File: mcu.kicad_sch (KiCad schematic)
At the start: 21 parts, among them J2 Conn_ARM_SWD_TagConnect_TC2030, SW1 SW_Push, U3 STM32L053R8Tx

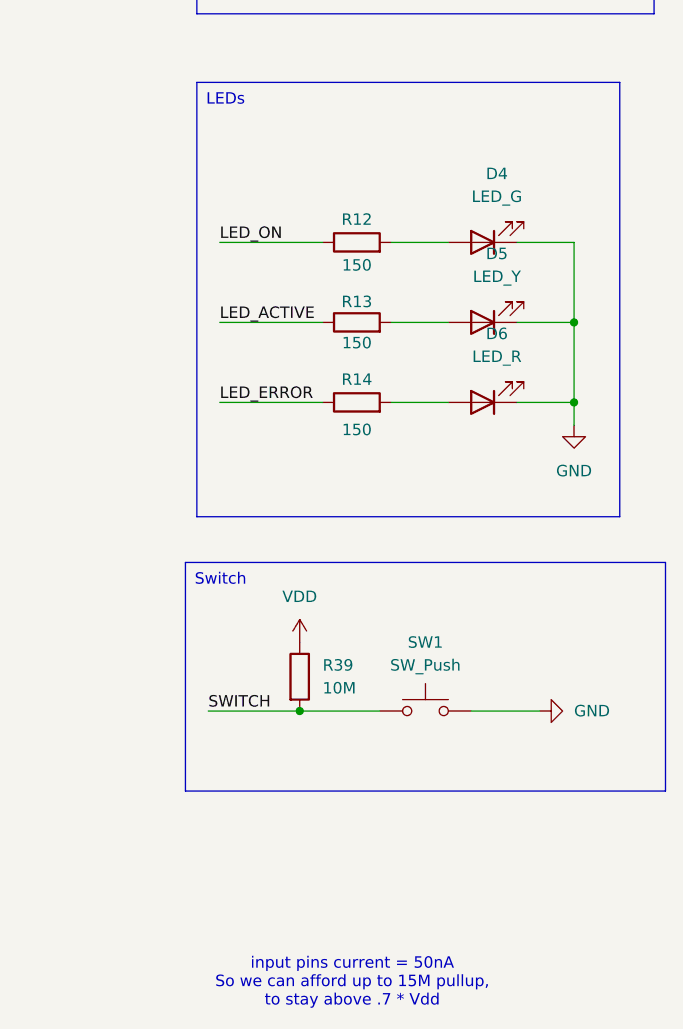
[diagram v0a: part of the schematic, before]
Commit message: Taking notes, doing some final adjustments to RC filter values
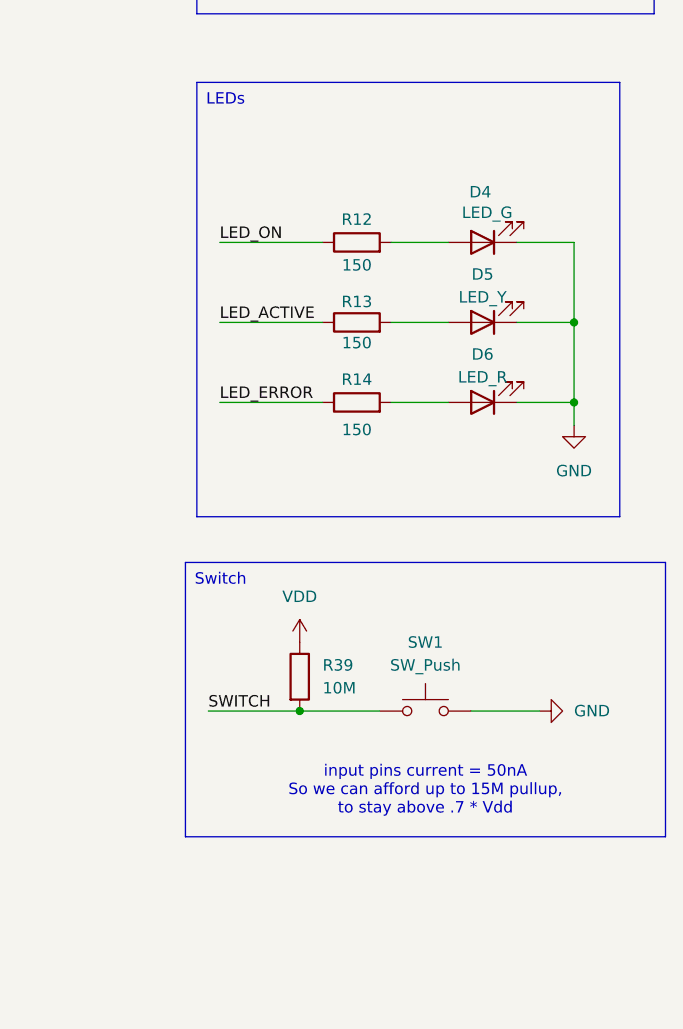
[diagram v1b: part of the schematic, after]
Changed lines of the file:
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@@
 		(exclude_from_sim no)
 		(at 220.98 104.14 0)
-		(size 53.34 25.4)
+		(size 53.34 30.48)
 		(stroke
 			(width 0)
@@
 	(text "input pins current = 50nA \nSo we can afford up to 15M pullup,\nto stay above .7 * Vdd"
 		(exclude_from_sim no)
-		(at 239.522 150.876 0)
+		(at 247.65 129.54 0)
 		(effects
 			(font
@@
 		(on_board yes)
 		(dnp no)
-		(fields_autoplaced yes)
 		(property "Reference" "D6"
-			(at 255.5875 78.74 0)
+			(at 254 81.026 0)
 			(effects
 				(font
@@
 		)
 		(property "Value" "LED_R"
-			(at 255.5875 81.28 0)
+			(at 254 83.566 0)
 			(effects
 				(font
@@
 		(on_board yes)
 		(dnp no)
-		(fields_autoplaced yes)
 		(property "Reference" "D4"
-			(at 255.5875 60.96 0)
+			(at 253.746 62.992 0)
 			(effects
 				(font
@@
 		)
 		(property "Value" "LED_G"
-			(at 255.5875 63.5 0)
+			(at 254.508 65.278 0)
 			(effects
 				(font
@@
 		(on_board yes)
 		(dnp no)
-		(fields_autoplaced yes)
 		(property "Reference" "D5"
-			(at 255.5875 69.85 0)
+			(at 254 72.136 0)
 			(effects
 				(font
@@
 		)
 		(property "Value" "LED_Y"
-			(at 255.5875 72.39 0)
-			(effects
-				(font
+			(at 254 74.676 0)
+			(effects
+				(font

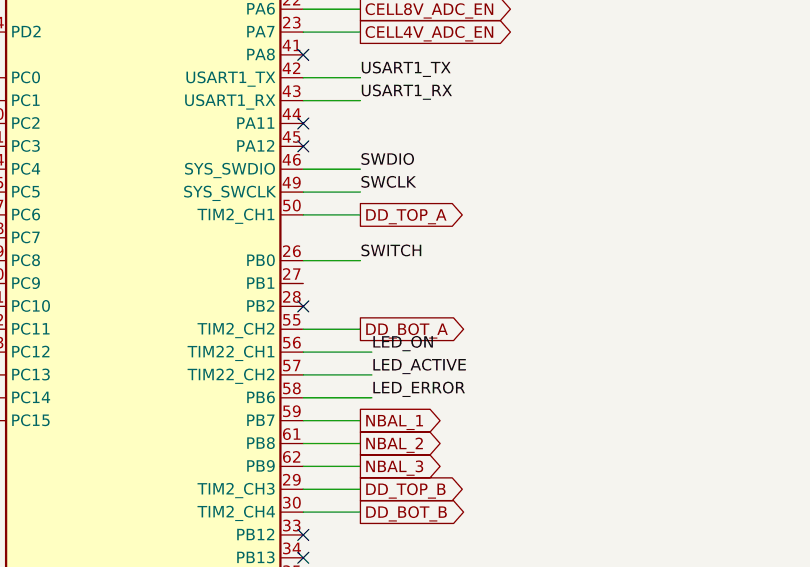
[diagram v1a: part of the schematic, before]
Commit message: L6388E mosfet drivers
Allow to enable/disable drivers
voltage dividers picked out
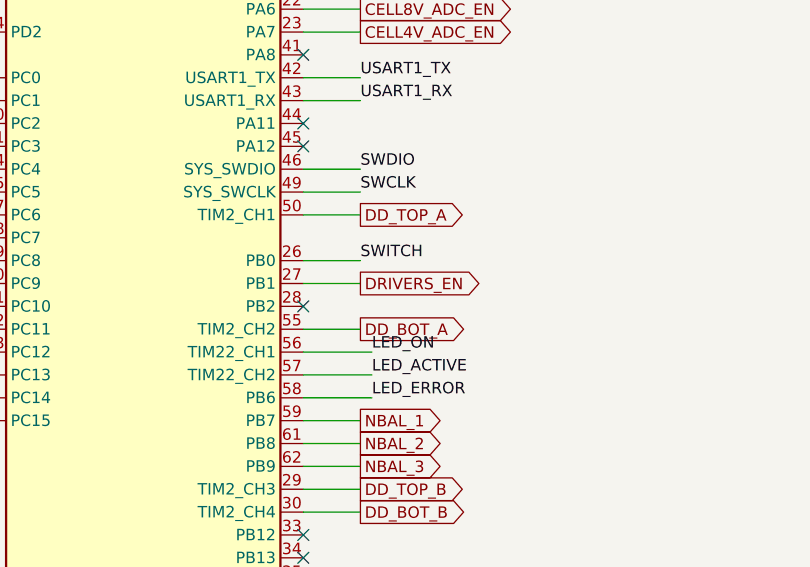
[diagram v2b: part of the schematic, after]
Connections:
- net DRIVERS_EN: now reaches U3.27 (PB1)
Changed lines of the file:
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@@
+	(wire
+		(pts
+			(xy 158.75 96.52) (xy 165.1 96.52)
+		)
+		(stroke
+			(width 0)
+			(type default)
+		)
+	)
 	(wire
 		(pts
@@
 			(effects
 				(font
+					(size 1.27 1.27)
+				)
+				(justify left)
+				(hide yes)
+			)
+		)
+	)
+	(global_label "DRIVERS_EN"
+		(shape output)
+		(at 165.1 96.52 0)
+		(fields_autoplaced yes)
+		(effects
+			(font
+				(size 1.27 1.27)
+			)
+			(justify left)
+		)
+		(property "Intersheetrefs" "${INTERSHEET_REFS}"
+			(at 179.3942 96.52 0)
+			(effects
+				(font

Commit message: New schematic done
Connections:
- net COMP2_INP: now reaches U3.17 (PA3)
- no-connect marks 31 -> 30

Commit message: A couple of part selections
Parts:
- R39: LCSC_Code (none) -> C26097
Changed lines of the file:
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@@
+			)
+		)
+		(property "LCSC_Code" "C26097"
+			(at 233.68 116.84 0)
+			(effects
+				(font
+					(size 1.27 1.27)
+				)
+				(hide yes)
 			)
 		)

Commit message: Layout
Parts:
- R39: footprint (none) -> Resistor_SMD:R_0603_1608Metric
- U3: LCSC_Code C784738 -> (none)
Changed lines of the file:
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@@
-			)
-		)
-		(property "LCSC_Code" "C784738"
-			(at 140.97 93.98 0)
-			(effects
-				(font
-					(size 1.27 1.27)
-				)
-				(hide yes)
-			)
-		)
-		(property "Sim.Device" ""
-			(at 140.97 93.98 0)
-			(effects
-				(font
-					(size 1.27 1.27)
-				)
-				(hide yes)
-			)
-		)
-		(property "Sim.Pins" ""
-			(at 140.97 93.98 0)
-			(effects
-				(font
-					(size 1.27 1.27)
-				)
-				(hide yes)
-			)
-		)
-		(property "Tolerance" ""
-			(at 140.97 93.98 0)
-			(effects
-				(font
-					(size 1.27 1.27)
-				)
-				(hide yes)
 			)
 		)
@@
 			)
 		)
-		(property "Footprint" ""
+		(property "Footprint" "Resistor_SMD:R_0603_1608Metric"
 			(at 231.902 116.84 90)
 			(effects

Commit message: Decent pass
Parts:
- renumbered C8 to C10, C9 to C11, C10 to C12, C11 to C13, C12 to C14, C21 to C15, C14 to C8, C13 to C9, D5 to D10, D6 to D11, D4 to D9, R13 to R10, R14 to R11, R39 to R8, R12 to R9
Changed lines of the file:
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@@
 		(dnp no)
 		(fields_autoplaced yes)
-		(property "Reference" "C10"
+		(property "Reference" "C12"
 			(at 252.73 29.2162 0)
 			(effects
@@
 			(project "JPBms2"
 				(path "/d86e471c-a8be-422d-a5d1-5a4699b7b766/852788cb-2266-4d4a-865c-a7e0873e4190"
-					(reference "C10")
+					(reference "C12")
 					(unit 1)
 				)
@@
 		(dnp no)
 		(fields_autoplaced yes)
-		(property "Reference" "#PWR022"
+		(property "Reference" "#PWR030"
 			(at 242.57 41.91 0)
 			(effects
@@
 			(project "JPBms2"
 				(path "/d86e471c-a8be-422d-a5d1-5a4699b7b766/852788cb-2266-4d4a-865c-a7e0873e4190"
-					(reference "#PWR022")
+					(reference "#PWR030")
 					(unit 1)
 				)
@@
 		(dnp no)
 		(fields_autoplaced yes)
-		(property "Reference" "#PWR027"
+		(property "Reference" "#PWR020"
 			(at 64.77 76.2 0)
 			(effects
@@
 			(project "JPBms2"
 				(path "/d86e471c-a8be-422d-a5d1-5a4699b7b766/852788cb-2266-4d4a-865c-a7e0873e4190"
-					(reference "#PWR027")
+					(reference "#PWR020")
 					(unit 1)
 				)
@@
 		(on_board yes)
 		(dnp no)
-		(property "Reference" "D6"
+		(property "Reference" "D11"
 			(at 254 81.026 0)
 			(effects
@@
 			(project "JPBms2"
 				(path "/d86e471c-a8be-422d-a5d1-5a4699b7b766/852788cb-2266-4d4a-865c-a7e0873e4190"
-					(reference "D6")
+					(reference "D11")
 					(unit 1)
 				)
@@
 		(dnp no)
 		(fields_autoplaced yes)
-		(property "Reference" "#PWR021"
+		(property "Reference" "#PWR027"
 			(at 148.59 29.21 0)
 			(effects
@@
 			(project "JPBms2"
 				(path "/d86e471c-a8be-422d-a5d1-5a4699b7b766/852788cb-2266-4d4a-865c-a7e0873e4190"
-					(reference "#PWR021")
+					(reference "#PWR027")
 					(unit 1)
 				)
@@
 		(on_board yes)
 		(dnp no)
-		(property "Reference" "#PWR019"
+		(property "Reference" "#PWR029"
 			(at 242.57 27.94 0)
 			(effects
@@
 			(project "JPBms2"
 				(path "/d86e471c-a8be-422d-a5d1-5a4699b7b766/852788cb-2266-4d4a-865c-a7e0873e4190"
-					(reference "#PWR019")
+					(reference "#PWR029")
 					(unit 1)
 				)
@@
 		(dnp no)
 		(fields_autoplaced yes)
-		(property "Reference" "C8"
+		(property "Reference" "C10"
 			(at 237.49 29.2099 0)
 			(effects
@@
 			(project "JPBms2"
 				(path "/d86e471c-a8be-422d-a5d1-5a4699b7b766/852788cb-2266-4d4a-865c-a7e0873e4190"
-					(reference "C8")
+					(reference "C10")
 					(unit 1)
 				)
@@
 		(dnp no)
 		(fields_autoplaced yes)
-		(property "Reference" "C11"
+		(property "Reference" "C13"
 			(at 259.08 29.2162 0)
 			(effects
@@
 			(project "JPBms2"
 				(path "/d86e471c-a8be-422d-a5d1-5a4699b7b766/852788cb-2266-4d4a-865c-a7e0873e4190"
-					(reference "C11")
+					(reference "C13")
 					(unit 1)
 				)
@@
 		(dnp no)
 		(fields_autoplaced yes)
-		(property "Reference" "#PWR023"
+		(property "Reference" "#PWR025"
 			(at 135.89 44.45 0)
 			(effects
@@
 			(project "JPBms2"
 				(path "/d86e471c-a8be-422d-a5d1-5a4699b7b766/852788cb-2266-4d4a-865c-a7e0873e4190"
-					(reference "#PWR023")
+					(reference "#PWR025")
 					(unit 1)
 				)
@@
 		(dnp no)
 		(fields_autoplaced yes)
-		(property "Reference" "C14"
+		(property "Reference" "C8"
 			(at 115.57 52.0762 0)
 			(effects
@@
 			(project "JPBms2"
 				(path "/d86e471c-a8be-422d-a5d1-5a4699b7b766/852788cb-2266-4d4a-865c-a7e0873e4190"
-					(reference "C14")
+					(reference "C8")
 					(unit 1)
 				)
@@
 		(dnp no)
 		(fields_autoplaced yes)
-		(property "Reference" "C9"
+		(property "Reference" "C11"
 			(at 245.11 29.2162 0)
 			(effects
@@
 			(project "JPBms2"
 				(path "/d86e471c-a8be-422d-a5d1-5a4699b7b766/852788cb-2266-4d4a-865c-a7e0873e4190"
-					(reference "C9")
+					(reference "C11")
 					(unit 1)
 				)
@@
 		(on_board yes)
 		(dnp no)
-		(property "Reference" "D4"
+		(property "Reference" "D9"
 			(at 253.746 62.992 0)
 			(effects
@@
 			(project "JPBms2"
 				(path "/d86e471c-a8be-422d-a5d1-5a4699b7b766/852788cb-2266-4d4a-865c-a7e0873e4190"
-					(reference "D4")
+					(reference "D9")
 					(unit 1)
 				)
@@
 		(dnp no)
 		(fields_autoplaced yes)
-		(property "Reference" "#PWR054"
+		(property "Reference" "#PWR031"
 			(at 266.7 120.65 0)
 			(effects
@@
 			(project "JPBms2"
 				(path "/d86e471c-a8be-422d-a5d1-5a4699b7b766/852788cb-2266-4d4a-865c-a7e0873e4190"
-					(reference "#PWR054")
+					(reference "#PWR031")
 					(unit 1)
 				)
@@
 		(dnp no)
 		(fields_autoplaced yes)
-		(property "Reference" "C12"
+		(property "Reference" "C14"
 			(at 264.16 29.2162 0)
 			(effects
@@
 			(project "JPBms2"
 				(path "/d86e471c-a8be-422d-a5d1-5a4699b7b766/852788cb-2266-4d4a-865c-a7e0873e4190"
-					(reference "C12")
+					(reference "C14")
 					(unit 1)
 				)
@@
 		(dnp no)
 		(fields_autoplaced yes)
-		(property "Reference" "#PWR020"
+		(property "Reference" "#PWR018"
 			(at 58.42 30.48 0)
 			(effects
@@
 			(project "JPBms2"
 				(path "/d86e471c-a8be-422d-a5d1-5a4699b7b766/852788cb-2266-4d4a-865c-a7e0873e4190"
-					(reference "#PWR020")
+					(reference "#PWR018")
 					(unit 1)
 				)
@@
 		(dnp no)
 		(fields_autoplaced yes)
-		(property "Reference" "#PWR028"
+		(property "Reference" "#PWR032"
 			(at 264.16 95.25 0)
 			(effects
@@
 			(project "JPBms2"
 				(path "/d86e471c-a8be-422d-a5d1-5a4699b7b766/852788cb-2266-4d4a-865c-a7e0873e4190"
-					(reference "#PWR028")
+					(reference "#PWR032")
 					(unit 1)
 				)
@@
 		(dnp no)
 		(fields_autoplaced yes)
-		(property "Reference" "C13"
+		(property "Reference" "C9"
 			(at 146.05 39.3638 0)
 			(effects
@@
 			(project "JPBms2"
 				(path "/d86e471c-a8be-422d-a5d1-5a4699b7b766/852788cb-2266-4d4a-865c-a7e0873e4190"
-					(reference "C13")
+					(reference "C9")
 					(unit 1)
 				)
@@
 		(dnp no)
 		(fields_autoplaced yes)
-		(property "Reference" "#PWR025"
+		(property "Reference" "#PWR023"
 			(at 113.03 62.23 0)
 			(effects
@@
 			(project "JPBms2"
 				(path "/d86e471c-a8be-422d-a5d1-5a4699b7b766/852788cb-2266-4d4a-865c-a7e0873e4190"
-					(reference "#PWR025")
+					(reference "#PWR023")
 					(unit 1)
 				)
@@
 		(dnp no)
 		(fields_autoplaced yes)
-		(property "Reference" "#PWR055"
+		(property "Reference" "#PWR028"
 			(at 233.68 116.84 0)
 			(effects
@@
 			(project "JPBms2"
 				(path "/d86e471c-a8be-422d-a5d1-5a4699b7b766/852788cb-2266-4d4a-865c-a7e0873e4190"
-					(reference "#PWR055")
+					(reference "#PWR028")
 					(unit 1)
 				)
@@
 		(dnp no)
 		(fields_autoplaced yes)
-		(property "Reference" "#PWR048"
+		(property "Reference" "#PWR022"
 			(at 74.93 83.82 0)
 			(effects
@@
 			(project "JPBms2"
 				(path "/d86e471c-a8be-422d-a5d1-5a4699b7b766/852788cb-2266-4d4a-865c-a7e0873e4190"
-					(reference "#PWR048")
+					(reference "#PWR022")
 					(unit 1)
 				)
@@
 		(on_board yes)
 		(dnp no)
-		(property "Reference" "D5"
+		(property "Reference" "D10"
 			(at 254 72.136 0)
 			(effects
@@
 			(project "JPBms2"
 				(path "/d86e471c-a8be-422d-a5d1-5a4699b7b766/852788cb-2266-4d4a-865c-a7e0873e4190"
-					(reference "D5")
+					(reference "D10")
 					(unit 1)
 				)
@@
 		(dnp no)
 		(fields_autoplaced yes)
-		(property "Reference" "#PWR024"
+		(property "Reference" "#PWR019"
 			(at 58.42 53.34 0)
 			(effects
@@
 			(project "JPBms2"
 				(path "/d86e471c-a8be-422d-a5d1-5a4699b7b766/852788cb-2266-4d4a-865c-a7e0873e4190"
-					(reference "#PWR024")
+					(reference "#PWR019")
 					(unit 1)
 				)
@@
 		(dnp no)
 		(fields_autoplaced yes)
-		(property "Reference" "#PWR029"
+		(property "Reference" "#PWR026"
 			(at 140.97 149.86 0)
 			(effects
@@
 			(project "JPBms2"
 				(path "/d86e471c-a8be-422d-a5d1-5a4699b7b766/852788cb-2266-4d4a-865c-a7e0873e4190"
-					(reference "#PWR029")
+					(reference "#PWR026")
 					(unit 1)
 				)
@@
 		(on_board yes)
 		(dnp no)
-		(property "Reference" "R14"
+		(property "Reference" "R11"
 			(at 240.03 83.82 90)
 			(effects
@@
 			(project "JPBms2"
 				(path "/d86e471c-a8be-422d-a5d1-5a4699b7b766/852788cb-2266-4d4a-865c-a7e0873e4190"
-					(reference "R14")
+					(reference "R11")
 					(unit 1)
 				)
@@
 		(dnp no)
 		(fields_autoplaced yes)
-		(property "Reference" "#PWR047"
+		(property "Reference" "#PWR021"
 			(at 71.12 83.82 0)
 			(effects
@@
 			(project "JPBms2"
 				(path "/d86e471c-a8be-422d-a5d1-5a4699b7b766/852788cb-2266-4d4a-865c-a7e0873e4190"
-					(reference "#PWR047")
+					(reference "#PWR021")
 					(unit 1)
 				)
@@
 		(dnp no)
 		(fields_autoplaced yes)
-		(property "Reference" "C21"
+		(property "Reference" "C15"
 			(at 267.97 29.2162 0)
 			(effects
@@
 			(project "JPBms2"
 				(path "/d86e471c-a8be-422d-a5d1-5a4699b7b766/852788cb-2266-4d4a-865c-a7e0873e4190"
-					(reference "C21")
+					(reference "C15")
 					(unit 1)
 				)
@@
 		(dnp no)
 		(fields_autoplaced yes)
-		(property "Reference" "R39"
+		(property "Reference" "R8"
 			(at 236.22 115.5699 0)
 			(effects
@@
 			(project "JPBms2"
 				(path "/d86e471c-a8be-422d-a5d1-5a4699b7b766/852788cb-2266-4d4a-865c-a7e0873e4190"
-					(reference "R39")
+					(reference "R8")
 					(unit 1)
 				)
@@
 		(on_board yes)
 		(dnp no)
-		(property "Reference" "#PWR026"
+		(property "Reference" "#PWR024"
 			(at 116.84 55.88 0)
 			(effects
@@
 			(project "JPBms2"
 				(path "/d86e471c-a8be-422d-a5d1-5a4699b7b766/852788cb-2266-4d4a-865c-a7e0873e4190"
-					(reference "#PWR026")
+					(reference "#PWR024")
 					(unit 1)
 				)
@@
 		(on_board yes)
 		(dnp no)
-		(property "Reference" "R12"
+		(property "Reference" "R9"
 			(at 240.03 66.04 90)
 			(effects
@@
 			(project "JPBms2"
 				(path "/d86e471c-a8be-422d-a5d1-5a4699b7b766/852788cb-2266-4d4a-865c-a7e0873e4190"
-					(reference "R12")
+					(reference "R9")
 					(unit 1)
 				)
@@
 		(on_board yes)
 		(dnp no)
-		(property "Reference" "R13"
+		(property "Reference" "R10"
 			(at 240.03 75.184 90)
 			(effects
@@
 			(project "JPBms2"
 				(path "/d86e471c-a8be-422d-a5d1-5a4699b7b766/852788cb-2266-4d4a-865c-a7e0873e4190"
-					(reference "R13")
+					(reference "R10")
 					(unit 1)
 				)
